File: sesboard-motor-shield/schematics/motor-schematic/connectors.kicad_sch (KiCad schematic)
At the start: 9 parts, among them J10 MOTOR_D_OUT, J11 STEPPER_TERMINAL, J3 Conn_01x20_Female, J4 Conn_01x20_Female, J5 SERVO1, J6 SERVO2, J7 MOTOR_A_OUT, J8 MOTOR_B_OUT, J9 MOTOR_C_OUT

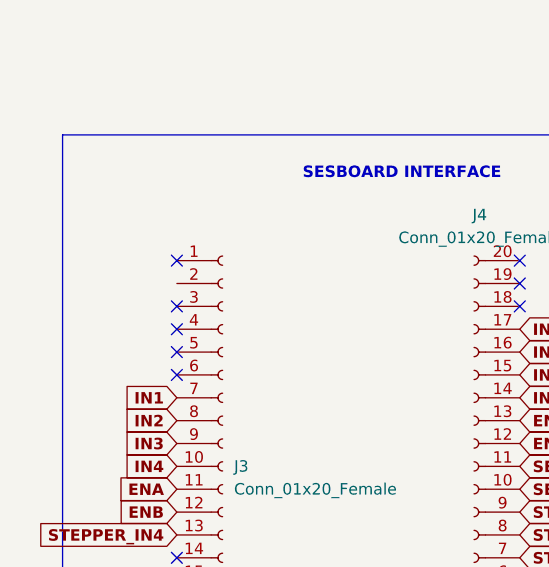
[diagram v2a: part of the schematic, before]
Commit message: added stepper connector
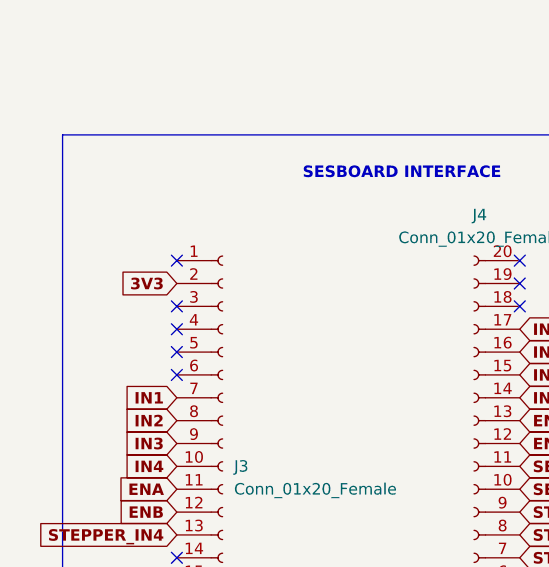
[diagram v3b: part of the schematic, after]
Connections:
- net 3V3: now reaches J3.2 (Pin_2)
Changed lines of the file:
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@@
+    )
+  )
+  (global_label "3V3" (shape input) (at 62.23 66.04 180) (fields_autoplaced)
+    (effects (font (size 1.27 1.27) bold) (justify right))
+    (property "Intersheet References" "${INTERSHEET_REFS}" (id 0) (at 56.1189 65.913 0)
+      (effects (font (size 1.27 1.27) bold) (justify right) hide)
     )
   )
